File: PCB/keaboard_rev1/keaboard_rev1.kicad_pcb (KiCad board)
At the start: 2 copper layers, 136.5 x 87.7 mm, 55 parts, among them K01 KEYSW, K02 KEYSW, K03 KEYSW, K04 KEYSW, K05 KEYSW, K06 KEYSW, K07 KEYSW, K08 KEYSW, K09 KEYSW, K10 KEYSW, K11 KEYSW, K12 KEYSW, K13 KEYSW, K14 KEYSW, K15 KEYSW, K16 KEYSW, K17 KEYSW, K18 KEYSW, K19 KEYSW, K20 KEYSW, K21 KEYSW, K22 KEYSW, K23 KEYSW, K24 KEYSW, K25 KEYSW, U1 ProMicro

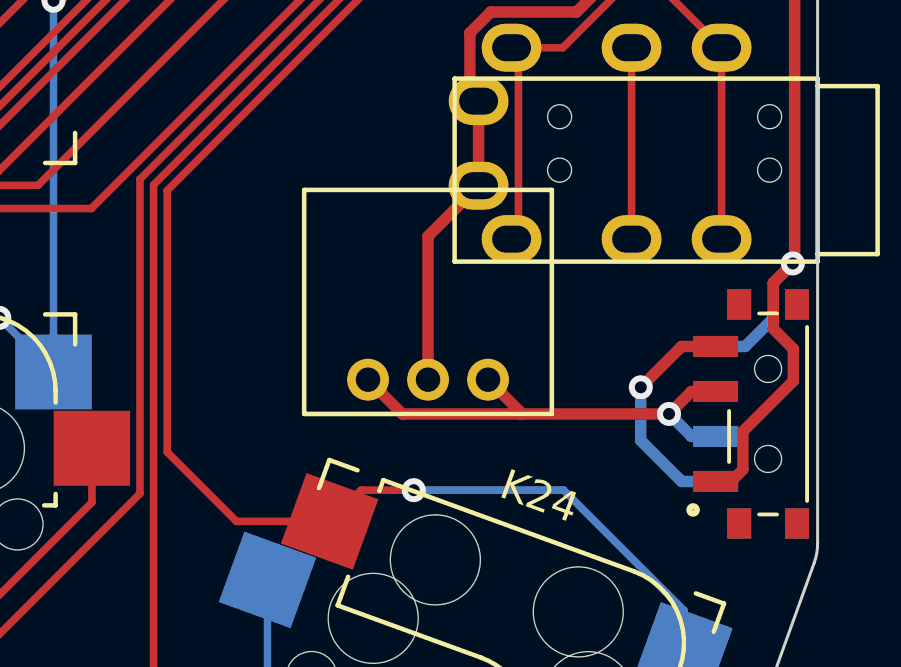
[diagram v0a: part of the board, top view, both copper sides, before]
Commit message: Move battery plug
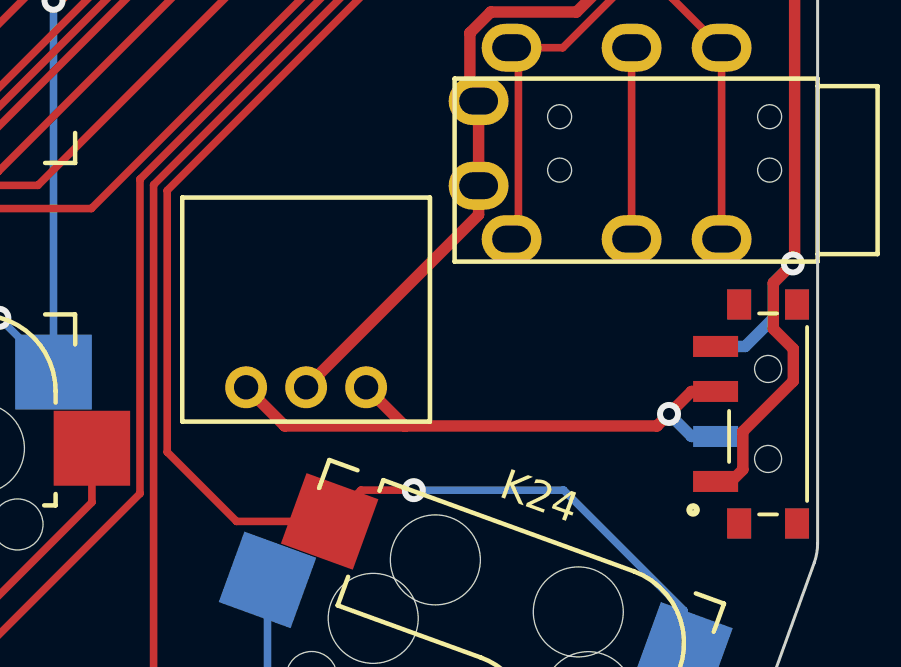
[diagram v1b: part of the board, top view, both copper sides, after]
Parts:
- moved BAT1 4.07 mm to (146.4, 75.6)
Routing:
- net Net-(SW_PWR1-Pad3): track 7.89 -> 0.00 mm, vias 1 -> 0
- net Net-(BAT1-Pad1): track 15.8 -> 20.4 mm
- net GND: track 103.0 -> 104.9 mm
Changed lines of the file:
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@@
     (thickness 1.6)
     (drawings 20)
-    (tracks 774)
+    (tracks 768)
     (zones 0)
     (modules 55)
@@
   )
   (module parts:DF3A-3P-2DS_reversible (layer F.Cu)
-    (at 150.495 75.311 180)
+    (at 146.431 75.565 180)
     (fp_text reference BAT1 (at -2 -2.54) (layer F.SilkS) hide
       (effects (font (size 1 1) (thickness 0.15)))
@@
   (segment (start 153.162 59.64416) (end 143.801021 69.005139) (width 0.254) (layer F.Cu) (net 12))
   (segment (start 153.162 45.847) (end 153.162 59.64416) (width 0.254) (layer F.Cu) (net 12))
-  (segment (start 160.949 74.204) (end 159.588 75.565) (width 0.381) (layer F.Cu) (net 13))
-  (segment (start 162.08 74.204) (end 160.949 74.204) (width 0.381) (layer F.Cu) (net 13))
-  (segment (start 159.588 75.565) (end 159.588 75.565) (width 0.381) (layer F.Cu) (net 13))
-  (via (at 159.588 75.565) (size 0.8) (drill 0.4) (layers F.Cu B.Cu) (net 13))
-  (segment (start 159.588 77.343) (end 159.588 75.565) (width 0.381) (layer B.Cu) (net 13))
-  (segment (start 160.949 78.704) (end 159.588 77.343) (width 0.381) (layer B.Cu) (net 13))
-  (segment (start 162.08 78.704) (end 160.949 78.704) (width 0.381) (layer B.Cu) (net 13))
   (segment (start 146.725801 31.880199) (end 146.669 31.937) (width 0.381) (layer B.Cu) (net 50))
   (segment (start 148.817065 31.880199) (end 146.725801 31.880199) (width 0.381) (layer B.Cu) (net 50))
@@
   (segment (start 161.838058 39.557) (end 161.909 39.557) (width 0.381) (layer F.Cu) (net 14))
   (segment (start 154.181 66.026) (end 153.89049 65.73549) (width 0.381) (layer F.Cu) (net 14))
-  (segment (start 152.495 70.532) (end 154.181 68.846) (width 0.381) (layer F.Cu) (net 14))
-  (segment (start 152.495 75.311) (end 152.495 70.532) (width 0.381) (layer F.Cu) (net 14))
+  (segment (start 154.181 69.815) (end 154.181 68.846) (width 0.381) (layer F.Cu) (net 14))
+  (segment (start 148.431 75.565) (end 154.181 69.815) (width 0.381) (layer F.Cu) (net 14))
   (segment (start 159.281 64.246) (end 159.281 70.626) (width 0.254) (layer F.Cu) (net 15))
   (segment (start 160.468 42.097) (end 149.927 42.097) (width 0.254) (layer B.Cu) (net 16))
@@
   (segment (start 161.278 77.204) (end 160.528 76.454) (width 0.381) (layer B.Cu) (net 49))
   (segment (start 162.08 77.204) (end 161.278 77.204) (width 0.381) (layer B.Cu) (net 49))
-  (segment (start 151.637999 76.454) (end 150.494999 75.311) (width 0.381) (layer F.Cu) (net 49))
-  (segment (start 155.575 76.390999) (end 155.575 76.454) (width 0.381) (layer F.Cu) (net 49))
-  (segment (start 154.495001 75.311) (end 155.575 76.390999) (width 0.381) (layer F.Cu) (net 49))
-  (segment (start 155.575 76.454) (end 151.637999 76.454) (width 0.381) (layer F.Cu) (net 49))
-  (segment (start 160.528 76.454) (end 155.575 76.454) (width 0.381) (layer F.Cu) (net 49))
+  (segment (start 147.719998 76.853999) (end 146.430999 75.565) (width 0.381) (layer F.Cu) (net 49))
+  (segment (start 160.528 76.454) (end 160.128001 76.853999) (width 0.381) (layer F.Cu) (net 49))
+  (segment (start 151.72 76.853999) (end 151.746001 76.853999) (width 0.381) (layer F.Cu) (net 49))
+  (segment (start 150.431001 75.565) (end 151.72 76.853999) (width 0.381) (layer F.Cu) (net 49))
+  (segment (start 151.746001 76.853999) (end 147.719998 76.853999) (width 0.381) (layer F.Cu) (net 49))
+  (segment (start 160.128001 76.853999) (end 151.746001 76.853999) (width 0.381) (layer F.Cu) (net 49))
 )

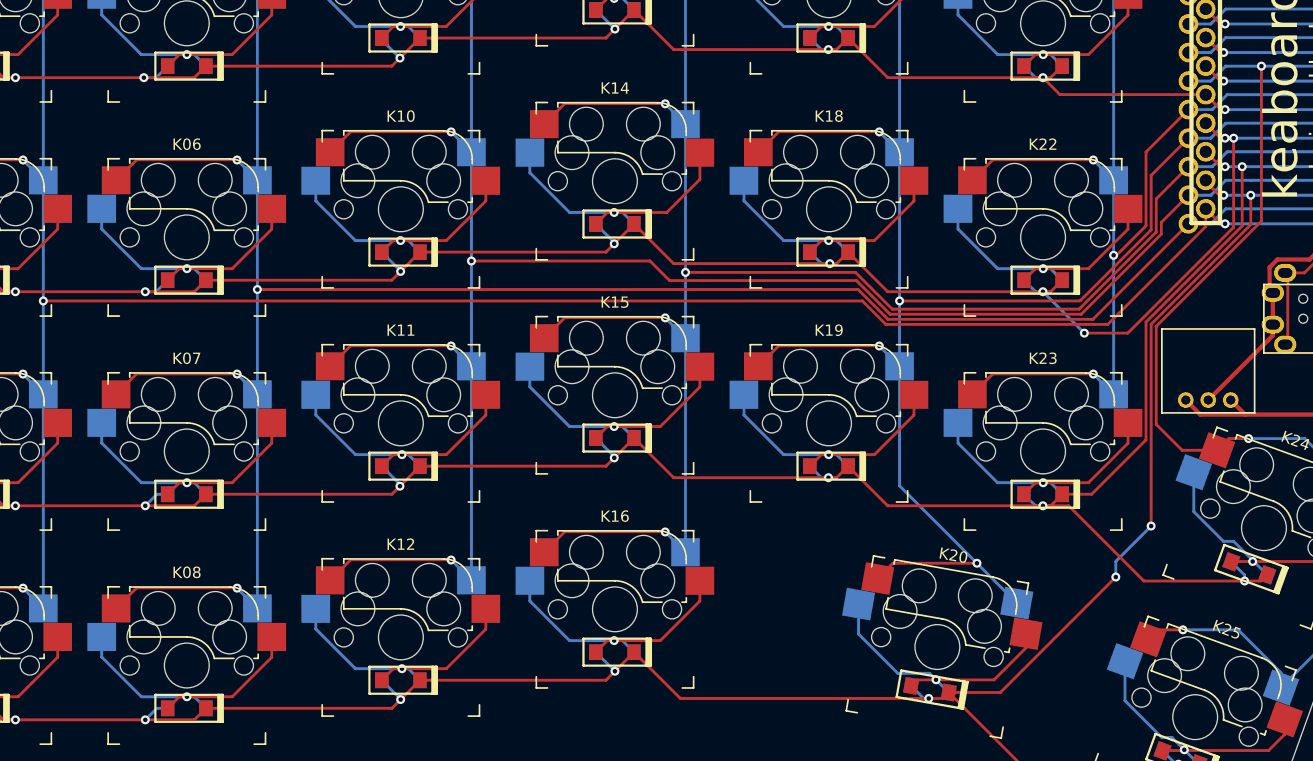
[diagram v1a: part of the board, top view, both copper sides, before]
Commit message: PDF schematic, add screw holes, update README
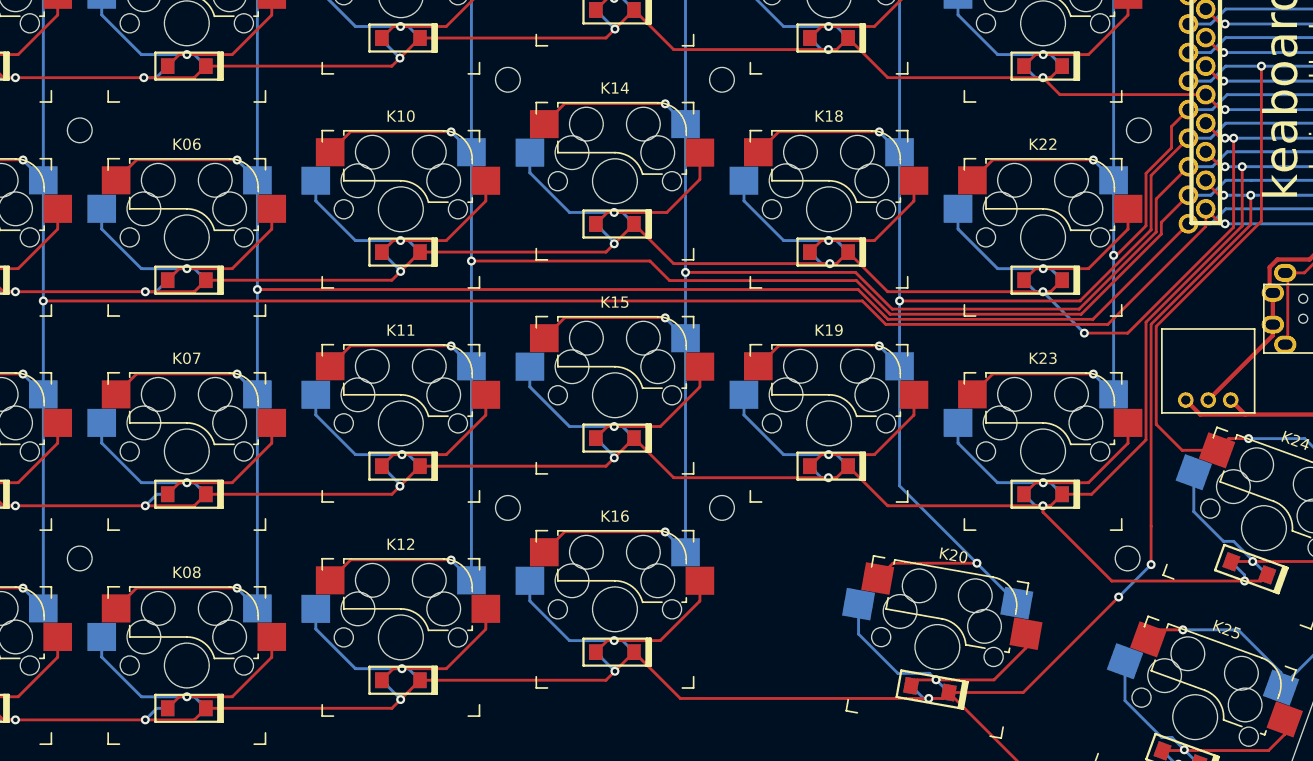
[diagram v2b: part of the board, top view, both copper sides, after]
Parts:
- added REF**: MountingHole_2.2mm_M2, MountingHole:MountingHole_2.2mm_M2, F.Cu at (105.2, 85.2)
- added REF**: MountingHole_2.2mm_M2, MountingHole:MountingHole_2.2mm_M2, F.Cu at (141.3, 89.7)
- added REF**: MountingHole_2.2mm_M2, MountingHole:MountingHole_2.2mm_M2, F.Cu at (86.1, 85.2)
- added REF**: MountingHole_2.2mm_M2, MountingHole:MountingHole_2.2mm_M2, F.Cu at (48.0, 89.7)
- added REF**: MountingHole_2.2mm_M2, MountingHole:MountingHole_2.2mm_M2, F.Cu at (142.3, 51.6)
- added REF**: MountingHole_2.2mm_M2, MountingHole:MountingHole_2.2mm_M2, F.Cu at (105.2, 47.1)
- added REF**: MountingHole_2.2mm_M2, MountingHole:MountingHole_2.2mm_M2, F.Cu at (86.1, 47.1)
- added REF**: MountingHole_2.2mm_M2, MountingHole:MountingHole_2.2mm_M2, F.Cu at (48.0, 51.6)
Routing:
- net ROW4: track 204.3 -> 205.5 mm

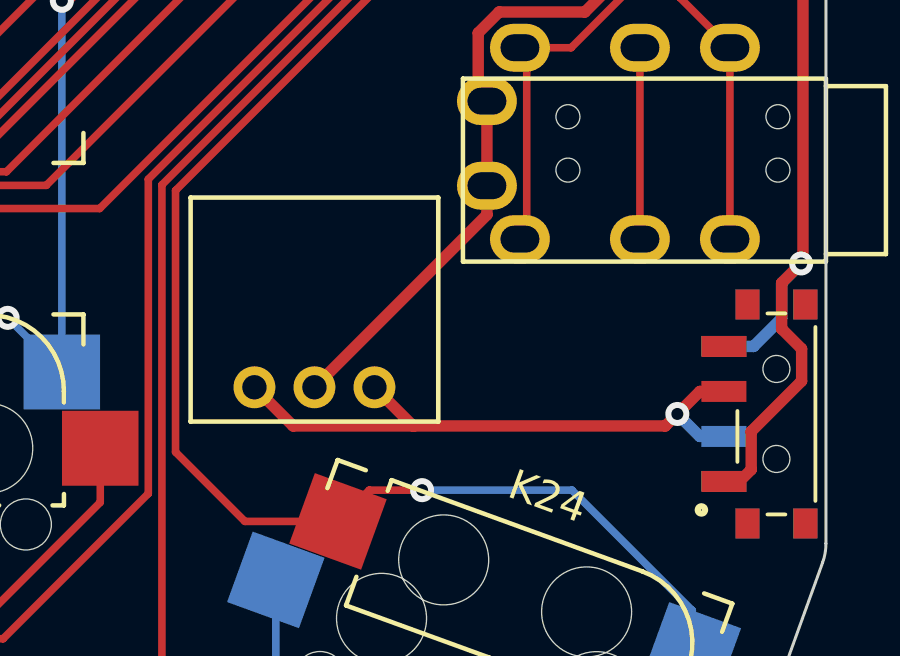
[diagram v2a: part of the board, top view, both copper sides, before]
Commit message: Add labels to battery plug, update battery plug footprint to correctly map pin holes, reroute traces to battery plug
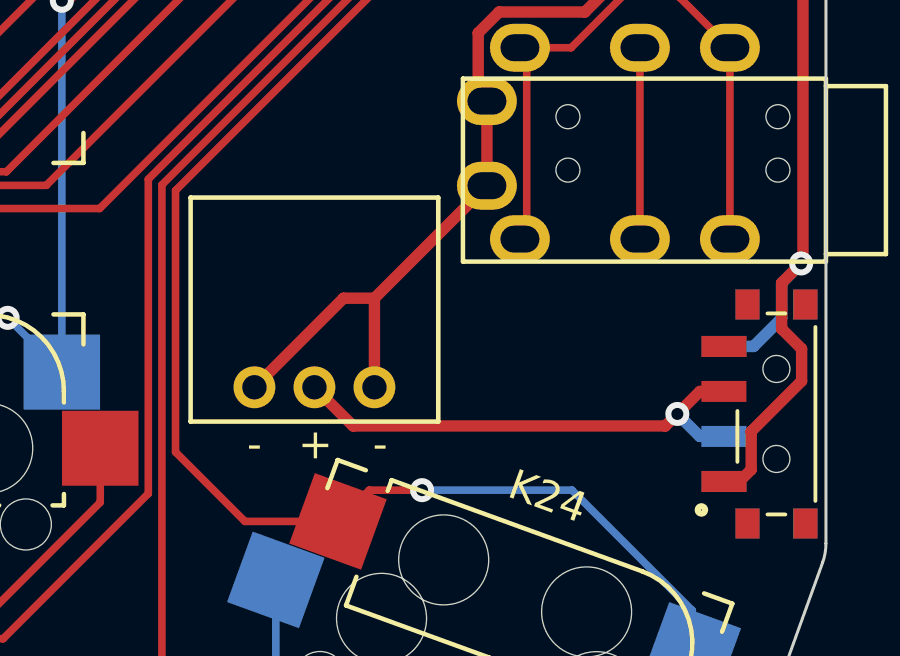
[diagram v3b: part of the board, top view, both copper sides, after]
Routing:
- net GND: track 104.9 -> 109.3 mm
- net Net-(BAT1-Pad1): track 20.4 -> 16.5 mm
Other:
- board text added: "+"
- board text added: "-"
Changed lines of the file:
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@@
   (general
     (thickness 1.6)
-    (drawings 20)
-    (tracks 771)
+    (drawings 23)
+    (tracks 770)
     (zones 0)
     (modules 63)
@@
     (add_net RAW)
   )
+  (module parts:DF3A-3P-2DS_reversible (layer F.Cu)
+    (at 146.431 75.565 180)
+    (fp_text reference BAT1 (at -2 -2.54) (layer F.SilkS) hide
+      (effects (font (size 1 1) (thickness 0.15)))
+    )
+    (fp_text value Battery (at -2 7.62) (layer F.SilkS) hide
+      (effects (font (size 1 1) (thickness 0.15)))
+    )
+    (fp_circle (center 0 1.905) (end 0.381 1.905) (layer F.Fab) (width 0.1524))
+    (fp_line (start 2.0005 -1.016) (end -6.0005 -1.016) (layer F.CrtYd) (width 0.1524))
+    (fp_line (start 2.0005 6.1976) (end 2.0005 -1.016) (layer F.CrtYd) (width 0.1524))
+    (fp_line (start -6.0005 6.1976) (end 2.0005 6.1976) (layer F.CrtYd) (width 0.1524))
+    (fp_line (start -6.0005 -1.016) (end -6.0005 6.1976) (layer F.CrtYd) (width 0.1524))
+    (fp_line (start 2.2545 -1.27) (end -6.2545 -1.27) (layer F.CrtYd) (width 0.1524))
+    (fp_line (start 2.2545 6.4516) (end 2.2545 -1.27) (layer F.CrtYd) (width 0.1524))
+    (fp_line (start -6.2545 6.4516) (end 2.2545 6.4516) (layer F.CrtYd) (width 0.1524))
+    (fp_line (start -6.2545 -1.27) (end -6.2545 6.4516) (layer F.CrtYd) (width 0.1524))
+    (fp_line (start -6.0005 -1.016) (end -6.0005 6.1976) (layer F.Fab) (width 0.1524))
+    (fp_line (start 2.0005 -1.016) (end -6.0005 -1.016) (layer F.Fab) (width 0.1524))
+    (fp_line (start 2.0005 6.1976) (end 2.0005 -1.016) (layer F.Fab) (width 0.1524))
+    (fp_line (start -6.0005 6.1976) (end 2.0005 6.1976) (layer F.Fab) (width 0.1524))
+    (fp_line (start -6.1275 -1.143) (end -6.1275 6.3246) (layer F.SilkS) (width 0.1524))
+    (fp_line (start 2.1275 -1.143) (end -6.1275 -1.143) (layer F.SilkS) (width 0.1524))
+    (fp_line (start 2.1275 6.3246) (end 2.1275 -1.143) (layer F.SilkS) (width 0.1524))
+    (fp_line (start -6.1275 6.3246) (end 2.1275 6.3246) (layer F.SilkS) (width 0.1524))
+    (fp_line (start 2.1275 6.3246) (end 2.1275 -1.143) (layer B.SilkS) (width 0.1524))
+    (fp_line (start 2.1275 -1.143) (end -6.1275 -1.143) (layer B.SilkS) (width 0.1524))
+    (fp_line (start -6.1275 -1.143) (end -6.1275 6.3246) (layer B.SilkS) (width 0.1524))
+    (fp_line (start -6.1275 6.3246) (end 2.1275 6.3246) (layer B.SilkS) (width 0.1524))
+    (pad 2 thru_hole circle (at -4.000001 0 180) (size 1.397 1.397) (drill 0.8128) (layers *.Cu *.Mask)
+      (net 14 GND))
+    (pad 1 thru_hole circle (at -2 0 180) (size 1.397 1.397) (drill 0.8128) (layers *.Cu *.Mask)
+      (net 49 "Net-(BAT1-Pad1)"))
+    (pad 2 thru_hole circle (at 0.000001 0 180) (size 1.397 1.397) (drill 0.8128) (layers *.Cu *.Mask)
+      (net 14 GND))
+  )
   (module MountingHole:MountingHole_2.2mm_M2 (layer F.Cu)
     (at 105.156 85.162)
@@
     (pad 1 np_thru_hole circle (at 0 0) (size 2.2 2.2) (drill 2.2) (layers *.Cu *.Mask))
   )
-  (module parts:DF3A-3P-2DS_reversible (layer F.Cu)
-    (at 146.431 75.565 180)
-    (fp_text reference BAT1 (at -2 -2.54) (layer F.SilkS) hide
-      (effects (font (size 1 1) (thickness 0.15)))
-    )
-    (fp_text value Battery (at -2 7.62) (layer F.SilkS) hide
-      (effects (font (size 1 1) (thickness 0.15)))
-    )
-    (fp_line (start -6.1275 6.3246) (end 2.1275 6.3246) (layer B.SilkS) (width 0.1524))
-    (fp_line (start -6.1275 -1.143) (end -6.1275 6.3246) (layer B.SilkS) (width 0.1524))
-    (fp_line (start 2.1275 -1.143) (end -6.1275 -1.143) (layer B.SilkS) (width 0.1524))
-    (fp_line (start 2.1275 6.3246) (end 2.1275 -1.143) (layer B.SilkS) (width 0.1524))
-    (fp_line (start -6.1275 6.3246) (end 2.1275 6.3246) (layer F.SilkS) (width 0.1524))
-    (fp_line (start 2.1275 6.3246) (end 2.1275 -1.143) (layer F.SilkS) (width 0.1524))
-    (fp_line (start 2.1275 -1.143) (end -6.1275 -1.143) (layer F.SilkS) (width 0.1524))
-    (fp_line (start -6.1275 -1.143) (end -6.1275 6.3246) (layer F.SilkS) (width 0.1524))
-    (fp_line (start -6.0005 6.1976) (end 2.0005 6.1976) (layer F.Fab) (width 0.1524))
-    (fp_line (start 2.0005 6.1976) (end 2.0005 -1.016) (layer F.Fab) (width 0.1524))
-    (fp_line (start 2.0005 -1.016) (end -6.0005 -1.016) (layer F.Fab) (width 0.1524))
-    (fp_line (start -6.0005 -1.016) (end -6.0005 6.1976) (layer F.Fab) (width 0.1524))
-    (fp_line (start -6.2545 -1.27) (end -6.2545 6.4516) (layer F.CrtYd) (width 0.1524))
-    (fp_line (start -6.2545 6.4516) (end 2.2545 6.4516) (layer F.CrtYd) (width 0.1524))
-    (fp_line (start 2.2545 6.4516) (end 2.2545 -1.27) (layer F.CrtYd) (width 0.1524))
-    (fp_line (start 2.2545 -1.27) (end -6.2545 -1.27) (layer F.CrtYd) (width 0.1524))
-    (fp_line (start -6.0005 -1.016) (end -6.0005 6.1976) (layer F.CrtYd) (width 0.1524))
-    (fp_line (start -6.0005 6.1976) (end 2.0005 6.1976) (layer F.CrtYd) (width 0.1524))
-    (fp_line (start 2.0005 6.1976) (end 2.0005 -1.016) (layer F.CrtYd) (width 0.1524))
-    (fp_line (start 2.0005 -1.016) (end -6.0005 -1.016) (layer F.CrtYd) (width 0.1524))
-    (fp_circle (center 0 1.905) (end 0.381 1.905) (layer F.Fab) (width 0.1524))
-    (pad 1 thru_hole circle (at -4.000001 0 180) (size 1.397 1.397) (drill 0.8128) (layers *.Cu *.Mask)
-      (net 49 "Net-(BAT1-Pad1)"))
-    (pad 2 thru_hole circle (at -2 0 180) (size 1.397 1.397) (drill 0.8128) (layers *.Cu *.Mask)
-      (net 14 GND))
-    (pad 1 thru_hole circle (at 0.000001 0 180) (size 1.397 1.397) (drill 0.8128) (layers *.Cu *.Mask)
-      (net 49 "Net-(BAT1-Pad1)"))
-  )
   (module parts:Kailh_socket_MX_reversible (layer B.Cu)
     (at 133.731 80.137 180)
@@
       (net 12 COL7))
   )
+  (gr_text - (at 146.431 77.47) (layer F.SilkS)
+    (effects (font (size 1 1) (thickness 0.2)))
+  )
+  (gr_text - (at 150.622 77.47) (layer F.SilkS)
+    (effects (font (size 1 1) (thickness 0.2)))
+  )
+  (gr_text + (at 148.463 77.47) (layer F.SilkS)
+    (effects (font (size 1 1) (thickness 0.2)))
+  )
   (gr_arc (start 163.59301 80.772001) (end 165.37101 81.407) (angle -19.65382589) (layer Edge.Cuts) (width 0.1))
   (gr_arc (start 69.088 29.591) (end 69.088 27.686) (angle -7.594647344) (layer Edge.Cuts) (width 0.1))
@@
   (segment (start 161.838058 39.557) (end 161.909 39.557) (width 0.381) (layer F.Cu) (net 14))
   (segment (start 154.181 66.026) (end 153.89049 65.73549) (width 0.381) (layer F.Cu) (net 14))
-  (segment (start 154.181 69.815) (end 154.181 68.846) (width 0.381) (layer F.Cu) (net 14))
-  (segment (start 148.431 75.565) (end 154.181 69.815) (width 0.381) (layer F.Cu) (net 14))
+  (segment (start 150.431001 72.595999) (end 154.181 68.846) (width 0.381) (layer F.Cu) (net 14))
+  (segment (start 150.431001 75.565) (end 150.431001 72.595999) (width 0.381) (layer F.Cu) (net 14))
+  (segment (start 149.4 72.595999) (end 150.431001 72.595999) (width 0.381) (layer F.Cu) (net 14))
+  (segment (start 146.430999 75.565) (end 149.4 72.595999) (width 0.381) (layer F.Cu) (net 14))
   (segment (start 159.281 64.246) (end 159.281 70.626) (width 0.254) (layer F.Cu) (net 15))
   (segment (start 160.468 42.097) (end 149.927 42.097) (width 0.254) (layer B.Cu) (net 16))
@@
   (segment (start 161.278 77.204) (end 160.528 76.454) (width 0.381) (layer B.Cu) (net 49))
   (segment (start 162.08 77.204) (end 161.278 77.204) (width 0.381) (layer B.Cu) (net 49))
-  (segment (start 147.719998 76.853999) (end 146.430999 75.565) (width 0.381) (layer F.Cu) (net 49))
+  (segment (start 149.719999 76.853999) (end 148.431 75.565) (width 0.381) (layer F.Cu) (net 49))
+  (segment (start 160.128001 76.853999) (end 149.719999 76.853999) (width 0.381) (layer F.Cu) (net 49))
   (segment (start 160.528 76.454) (end 160.128001 76.853999) (width 0.381) (layer F.Cu) (net 49))
-  (segment (start 151.72 76.853999) (end 151.746001 76.853999) (width 0.381) (layer F.Cu) (net 49))
-  (segment (start 150.431001 75.565) (end 151.72 76.853999) (width 0.381) (layer F.Cu) (net 49))
-  (segment (start 151.746001 76.853999) (end 147.719998 76.853999) (width 0.381) (layer F.Cu) (net 49))
-  (segment (start 160.128001 76.853999) (end 151.746001 76.853999) (width 0.381) (layer F.Cu) (net 49))
 )

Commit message: Update pcb image, generate gerber
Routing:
- net GND: track 109.3 -> 110.7 mm, vias 4 -> 6
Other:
- board text added: "on >"
